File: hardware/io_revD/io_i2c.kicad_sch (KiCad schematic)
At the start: 50 parts, among them J1 Target Interface, 2716 Pinout, J2 Jumper Block, J3 Jumper Block, J4 Target Interface, 2716 Pinout, Q1 2N7000, U1 2716, U2 74HCT74, U3 74HCT125, U4 74HCT138, U6 MCP23018-E_SP, U7 74HCT138

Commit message: fixed pullup
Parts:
- removed R?: 1k, Resistor_THT:R_Axial_DIN0207_L6.3mm_D2.5mm_P2.54mm_Vertical, symbol Device:R
- added R?: 1k, Resistor_THT:R_Axial_DIN0207_L6.3mm_D2.5mm_P2.54mm_Vertical, symbol Device:R
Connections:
- net +5V: now also R?.1
- net at D1.2 (A), D2.2 (A), D3.2 (A)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: now also R?.2
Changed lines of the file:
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@@
   (junction (at 180.975 215.9) (diameter 0) (color 0 0 0 0)
   )
+  (junction (at 151.13 139.065) (diameter 0) (color 0 0 0 0)
+  )
   (junction (at 212.09 133.985) (diameter 0) (color 0 0 0 0)
   )
@@
   )
   (junction (at 185.42 80.645) (diameter 0) (color 0 0 0 0)
-  )
-  (junction (at 134.62 163.83) (diameter 0) (color 0 0 0 0)
   )
   (junction (at 212.09 159.385) (diameter 0) (color 0 0 0 0)
@@
     (stroke (width 0) (type default) (color 0 0 0 0))
   )
-  (wire (pts (xy 130.81 163.83) (xy 134.62 163.83))
-    (stroke (width 0) (type default) (color 0 0 0 0))
-  )
   (wire (pts (xy 246.38 32.385) (xy 246.38 33.655))
     (stroke (width 0) (type default) (color 0 0 0 0))
@@
     (stroke (width 0) (type default) (color 0 0 0 0))
   )
-  (wire (pts (xy 134.62 163.83) (xy 138.43 163.83))
+  (wire (pts (xy 130.81 163.83) (xy 138.43 163.83))
     (stroke (width 0) (type default) (color 0 0 0 0))
   )
@@
     (pin "1")
   )
-  (symbol (lib_id "power:+5V") (at 134.62 156.21 0) (unit 1)
-    (in_bom yes) (on_board yes)
-    (property "Reference" "#PWR?" (id 0) (at 134.62 160.02 0)
-      (effects (font (size 1.27 1.27)) hide)
-    )
-    (property "Value" "+5V" (id 1) (at 135.001 151.8158 0))
-    (property "Footprint" "" (id 2) (at 134.62 156.21 0)
-      (effects (font (size 1.27 1.27)) hide)
-    )
-    (property "Datasheet" "" (id 3) (at 134.62 156.21 0)
-      (effects (font (size 1.27 1.27)) hide)
-    )
-    (pin "1")
-  )
   (symbol (lib_id "74xx:74LS125") (at 43.815 76.2 0) (unit 2)
     (in_bom yes) (on_board yes)
@@
     )
     (pin "1")
+  )
+  (symbol (lib_id "Device:R") (at 151.13 135.255 0) (unit 1)
+    (in_bom yes) (on_board yes)
+    (property "Reference" "R?" (id 0) (at 147.32 133.985 0)
+      (effects (font (size 1.27 1.27)) (justify left))
+    )
+    (property "Value" "1k" (id 1) (at 147.32 136.525 0)
+      (effects (font (size 1.27 1.27)) (justify left))
+    )
+    (property "Footprint" "Resistor_THT:R_Axial_DIN0207_L6.3mm_D2.5mm_P2.54mm_Vertical" (id 2) (at 149.352 135.255 90)
+      (effects (font (size 1.27 1.27)) hide)
+    )
+    (property "Datasheet" "~" (id 3) (at 151.13 135.255 0)
+      (effects (font (size 1.27 1.27)) hide)
+    )
+    (pin "1")
+    (pin "2")
   )
   (symbol (lib_id "Diode:1N4148") (at 172.085 226.06 0) (unit 1)
@@
     (pin "1")
   )
-  (symbol (lib_id "Device:R") (at 134.62 160.02 0) (unit 1)
-    (in_bom yes) (on_board yes)
-    (property "Reference" "R?" (id 0) (at 130.81 158.75 0)
-      (effects (font (size 1.27 1.27)) (justify left))
-    )
-    (property "Value" "1k" (id 1) (at 130.81 161.29 0)
-      (effects (font (size 1.27 1.27)) (justify left))
-    )
-    (property "Footprint" "Resistor_THT:R_Axial_DIN0207_L6.3mm_D2.5mm_P2.54mm_Vertical" (id 2) (at 132.842 160.02 90)
-      (effects (font (size 1.27 1.27)) hide)
-    )
-    (property "Datasheet" "~" (id 3) (at 134.62 160.02 0)
-      (effects (font (size 1.27 1.27)) hide)
-    )
-    (pin "1")
-    (pin "2")
-  )
   (symbol (lib_id "Device:R") (at 232.41 91.44 0) (unit 1)
     (in_bom yes) (on_board yes)
@@
     )
     (property "Datasheet" "" (id 3) (at 102.87 61.595 0)
+      (effects (font (size 1.27 1.27)) hide)
+    )
+    (pin "1")
+  )
+  (symbol (lib_id "power:+5V") (at 151.13 131.445 0) (unit 1)
+    (in_bom yes) (on_board yes)
+    (property "Reference" "#PWR?" (id 0) (at 151.13 135.255 0)
+      (effects (font (size 1.27 1.27)) hide)
+    )
+    (property "Value" "+5V" (id 1) (at 151.511 127.0508 0))
+    (property "Footprint" "" (id 2) (at 151.13 131.445 0)
+      (effects (font (size 1.27 1.27)) hide)
+    )
+    (property "Datasheet" "" (id 3) (at 151.13 131.445 0)
       (effects (font (size 1.27 1.27)) hide)
     )
@@
       (reference "#PWR?") (unit 1) (value "GND") (footprint "")
     )
-    (path "/1f6a280c-02f7-41a2-af9f-44fb04f0a9b2"
-      (reference "#PWR?") (unit 1) (value "+5V") (footprint "")
-    )
     (path "/43879ac7-f230-4696-95ed-6babb22f0407"
       (reference "#PWR?") (unit 1) (value "+5V") (footprint "")
@@
       (reference "#PWR?") (unit 1) (value "+5V") (footprint "")
     )
+    (path "/8a404b86-d3e1-4be0-a8ba-be524434abfb"
+      (reference "#PWR?") (unit 1) (value "+5V") (footprint "")
+    )
     (path "/9147cd62-9ca6-4c6a-bf66-316c793b7506"
       (reference "#PWR?") (unit 1) (value "+5VD") (footprint "")
@@
       (reference "R5") (unit 1) (value "10k") (footprint "Resistor_THT:R_Axial_DIN0207_L6.3mm_D2.5mm_P2.54mm_Vertical")
     )
+    (path "/5191daa9-7512-4ab7-ba71-5f4cad956e0f"
+      (reference "R?") (unit 1) (value "1k") (footprint "Resistor_THT:R_Axial_DIN0207_L6.3mm_D2.5mm_P2.54mm_Vertical")
+    )
     (path "/59d70ba8-8901-43d7-9e71-45fc4d05f5dd"
       (reference "R?") (unit 1) (value "10k") (footprint "Resistor_THT:R_Axial_DIN0207_L6.3mm_D2.5mm_P2.54mm_Vertical")
@@
       (reference "R?") (unit 1) (value "4.7k") (footprint "Resistor_THT:R_Axial_DIN0207_L6.3mm_D2.5mm_P2.54mm_Vertical")
     )
-    (path "/857b2b5c-6887-40fa-8781-7287c485d91d"
-      (reference "R?") (unit 1) (value "1k") (footprint "Resistor_THT:R_Axial_DIN0207_L6.3mm_D2.5mm_P2.54mm_Vertical")
-    )
     (path "/00000000-0000-0000-0000-0000607df9f3"

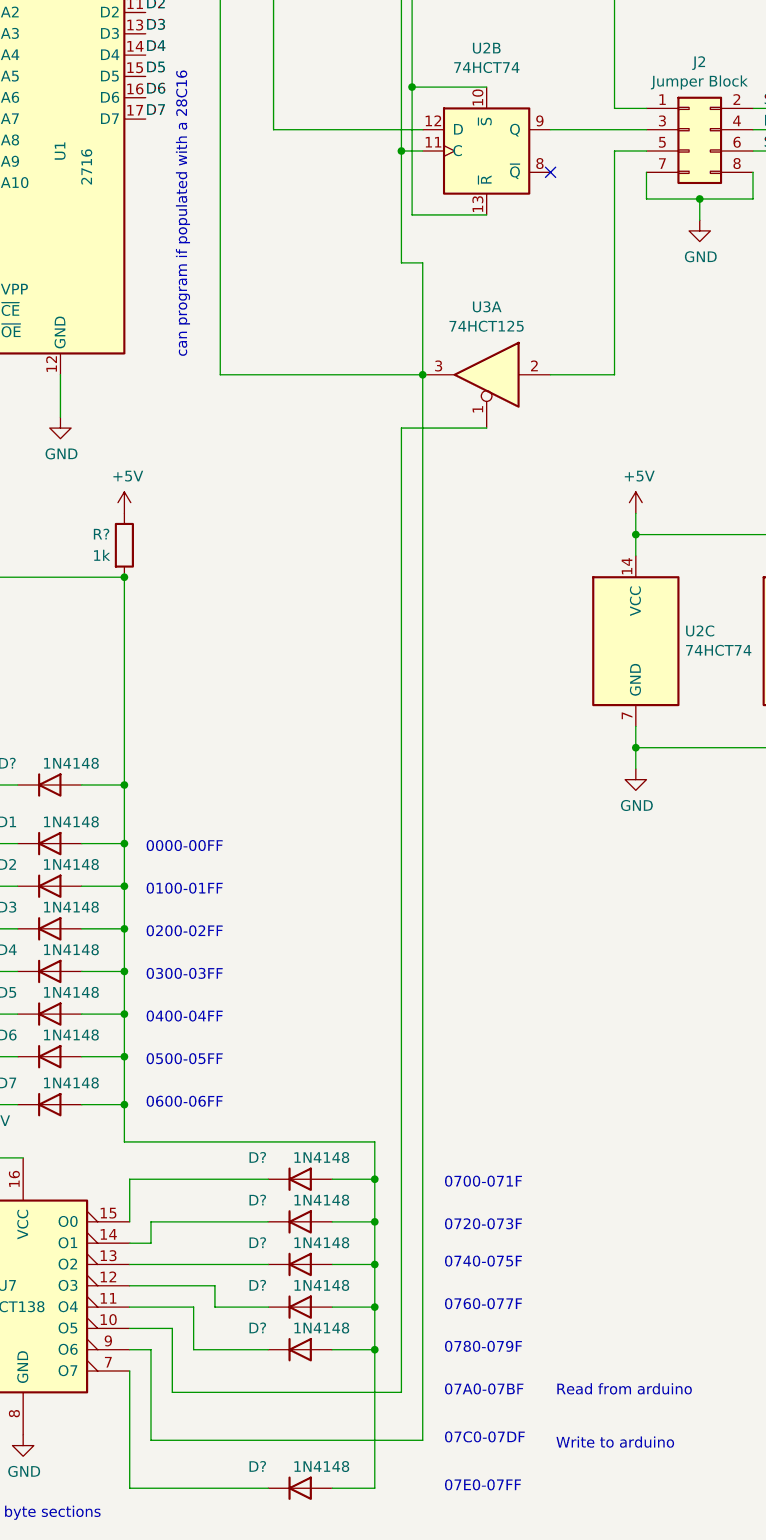
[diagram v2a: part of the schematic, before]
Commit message: fix crossed wires
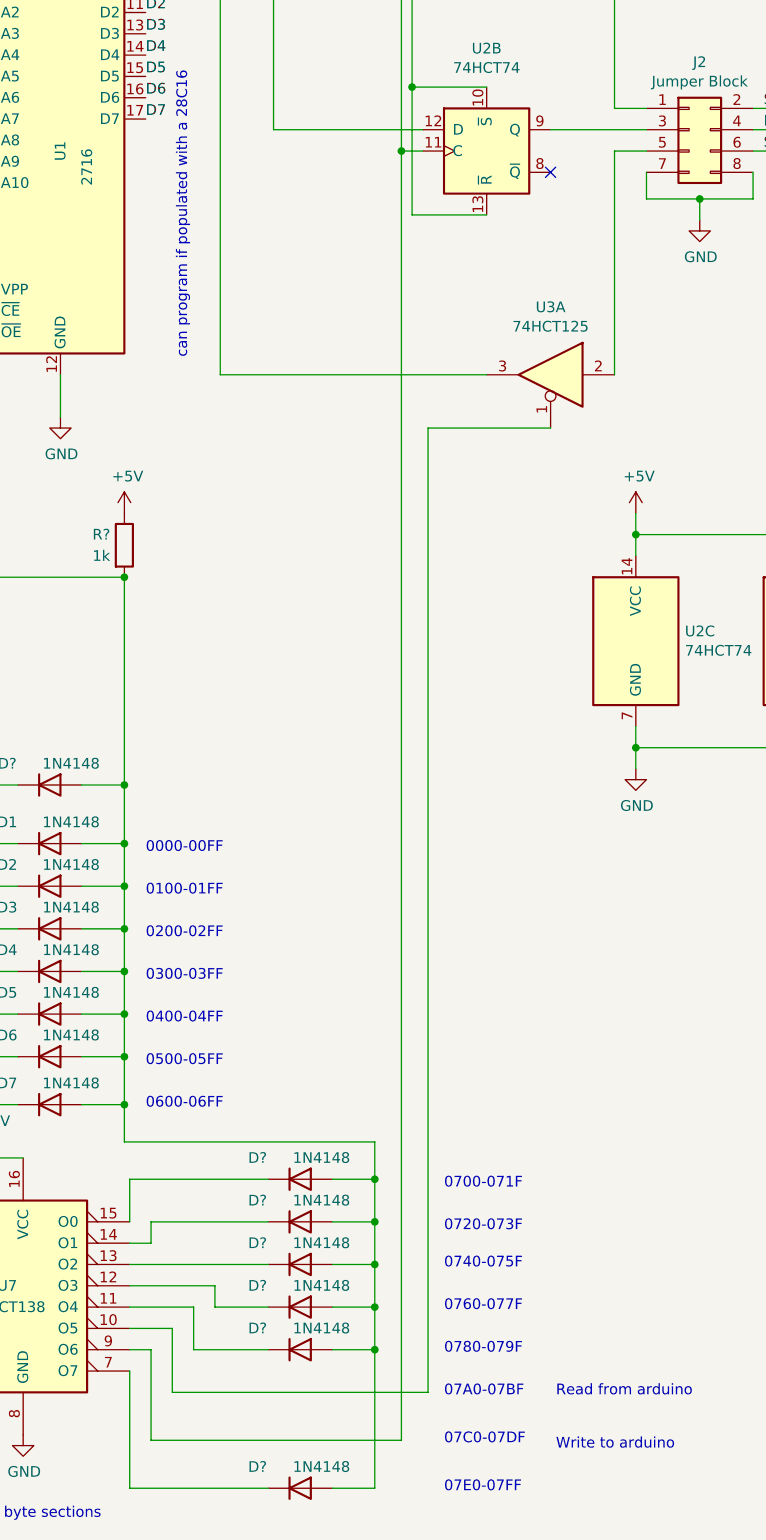
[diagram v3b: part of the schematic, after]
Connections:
- net D0: no longer U2.11 (C), U2.3 (C), U7.9 (O6)
- new net: U2.11 (C), U2.3 (C), U7.9 (O6)
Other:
- moved on the sheet: U3A
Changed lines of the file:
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@@
   (junction (at 252.73 93.345) (diameter 0) (color 0 0 0 0)
-  )
-  (junction (at 186.69 114.935) (diameter 0) (color 0 0 0 0)
   )
   (junction (at 180.975 215.9) (diameter 0) (color 0 0 0 0)
@@
     (stroke (width 0) (type default) (color 0 0 0 0))
   )
-  (wire (pts (xy 186.69 114.935) (xy 186.69 241.935))
-    (stroke (width 0) (type default) (color 0 0 0 0))
-  )
   (wire (pts (xy 256.54 156.21) (xy 262.89 156.21))
     (stroke (width 0) (type default) (color 0 0 0 0))
@@
     (stroke (width 0) (type default) (color 0 0 0 0))
   )
-  (wire (pts (xy 184.15 121.285) (xy 194.31 121.285))
-    (stroke (width 0) (type default) (color 0 0 0 0))
-  )
   (wire (pts (xy 154.305 218.44) (xy 154.305 215.9))
     (stroke (width 0) (type default) (color 0 0 0 0))
@@
     (stroke (width 0) (type default) (color 0 0 0 0))
   )
-  (wire (pts (xy 186.69 101.6) (xy 186.69 114.935))
-    (stroke (width 0) (type default) (color 0 0 0 0))
-  )
   (wire (pts (xy 92.71 109.855) (xy 90.17 109.855))
     (stroke (width 0) (type default) (color 0 0 0 0))
@@
     (stroke (width 0) (type default) (color 0 0 0 0))
   )
-  (wire (pts (xy 201.93 114.935) (xy 209.55 114.935))
-    (stroke (width 0) (type default) (color 0 0 0 0))
-  )
   (wire (pts (xy 212.09 156.845) (xy 212.09 159.385))
     (stroke (width 0) (type default) (color 0 0 0 0))
@@
     (stroke (width 0) (type default) (color 0 0 0 0))
   )
-  (wire (pts (xy 162.56 114.935) (xy 186.69 114.935))
+  (wire (pts (xy 162.56 114.935) (xy 194.31 114.935))
     (stroke (width 0) (type default) (color 0 0 0 0))
   )
@@
     (stroke (width 0) (type default) (color 0 0 0 0))
   )
-  (wire (pts (xy 184.15 236.22) (xy 184.15 121.285))
-    (stroke (width 0) (type default) (color 0 0 0 0))
-  )
   (wire (pts (xy 71.755 139.065) (xy 81.915 139.065))
     (stroke (width 0) (type default) (color 0 0 0 0))
@@
     (stroke (width 0) (type default) (color 0 0 0 0))
   )
-  (wire (pts (xy 184.15 101.6) (xy 186.69 101.6))
+  (wire (pts (xy 201.93 121.285) (xy 187.325 121.285))
     (stroke (width 0) (type default) (color 0 0 0 0))
   )
@@
     (stroke (width 0) (type default) (color 0 0 0 0))
   )
+  (wire (pts (xy 184.15 88.265) (xy 184.15 241.935))
+    (stroke (width 0) (type default) (color 0 0 0 0))
+  )
   (wire (pts (xy 151.13 201.93) (xy 151.13 196.215))
     (stroke (width 0) (type default) (color 0 0 0 0))
   )
+  (wire (pts (xy 187.325 121.285) (xy 187.325 236.22))
+    (stroke (width 0) (type default) (color 0 0 0 0))
+  )
   (wire (pts (xy 57.785 131.445) (xy 64.135 131.445))
     (stroke (width 0) (type default) (color 0 0 0 0))
@@
     (stroke (width 0) (type default) (color 0 0 0 0))
   )
-  (wire (pts (xy 184.15 88.265) (xy 184.15 101.6))
-    (stroke (width 0) (type default) (color 0 0 0 0))
-  )
   (wire (pts (xy 120.015 131.445) (xy 120.015 144.145))
     (stroke (width 0) (type default) (color 0 0 0 0))
@@
     (stroke (width 0) (type default) (color 0 0 0 0))
   )
-  (wire (pts (xy 156.845 236.22) (xy 184.15 236.22))
+  (wire (pts (xy 156.845 236.22) (xy 187.325 236.22))
     (stroke (width 0) (type default) (color 0 0 0 0))
   )
@@
     (stroke (width 0) (type default) (color 0 0 0 0))
   )
-  (wire (pts (xy 154.305 241.935) (xy 186.69 241.935))
+  (wire (pts (xy 154.305 241.935) (xy 184.15 241.935))
     (stroke (width 0) (type default) (color 0 0 0 0))
   )
@@
     (pin "9")
   )
-  (symbol (lib_id "74xx:74LS125") (at 194.31 114.935 0) (mirror y) (unit 1)
+  (symbol (lib_id "74xx:74LS125") (at 201.93 114.935 0) (mirror y) (unit 1)
     (in_bom yes) (on_board yes)
-    (property "Reference" "U3" (id 0) (at 194.31 106.8832 0))
-    (property "Value" "74HCT125" (id 1) (at 194.31 109.1946 0))
-    (property "Footprint" "Package_DIP:DIP-14_W7.62mm" (id 2) (at 194.31 114.935 0)
-      (effects (font (size 1.27 1.27)) hide)
-    )
-    (property "Datasheet" "http://www.ti.com/lit/gpn/sn74LS125" (id 3) (at 194.31 114.935 0)
-      (effects (font (size 1.27 1.27)) hide)
-    )
+    (property "Reference" "U3" (id 0) (at 201.93 106.8832 0))
+    (property "Value" "74HCT125" (id 1) (at 201.93 109.1946 0))
+    (property "Footprint" "Package_DIP:DIP-14_W7.62mm" (id 2) (at 201.93 114.935 0)
+      (effects (font (size 1.27 1.27)) hide)
+    )
+    (property "Datasheet" "http://www.ti.com/lit/gpn/sn74LS125" (id 3) (at 201.93 114.935 0)
+      (effects (font (size 1.27 1.27)) hide)
+    )

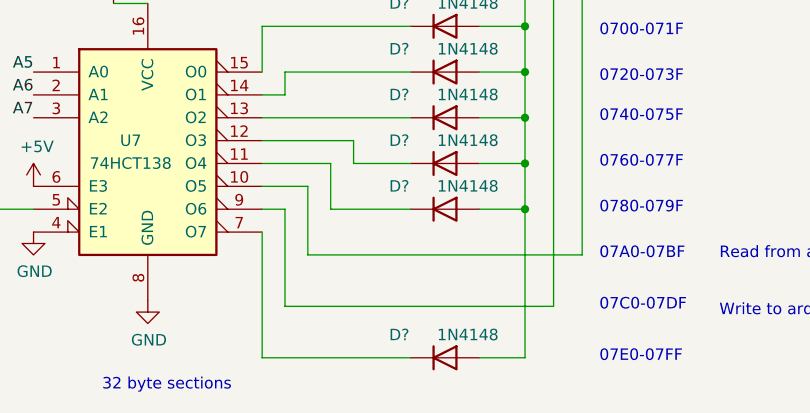
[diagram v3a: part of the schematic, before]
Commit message: diode fix for decoding writes
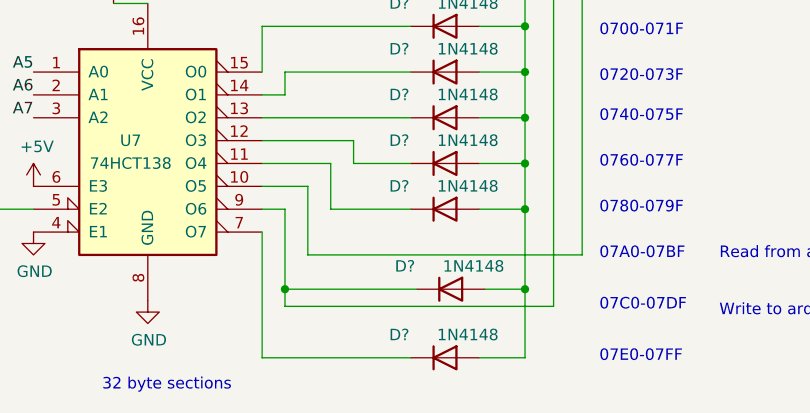
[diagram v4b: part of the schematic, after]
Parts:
- added D?: 1N4148, Diode_THT:D_DO-35_SOD27_P2.54mm_Vertical_AnodeUp, symbol Diode:1N4148
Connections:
- net at D1.2 (A), D2.2 (A), D3.2 (A)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: now also D?.2 (A)
- net at U2.11 (C), U2.3 (C), U7.9 (O6): now also D?.1 (K)
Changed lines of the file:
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@@
   (junction (at 212.09 133.985) (diameter 0) (color 0 0 0 0)
   )
+  (junction (at 154.305 240.03) (diameter 0) (color 0 0 0 0)
+  )
   (junction (at 125.73 104.775) (diameter 0) (color 0 0 0 0)
   )
@@
   )
   (junction (at 151.13 196.215) (diameter 0) (color 0 0 0 0)
+  )
+  (junction (at 180.975 240.03) (diameter 0) (color 0 0 0 0)
   )
   (junction (at 151.13 191.135) (diameter 0) (color 0 0 0 0)
@@
     (stroke (width 0) (type default) (color 0 0 0 0))
   )
+  (wire (pts (xy 154.305 240.03) (xy 154.305 231.14))
+    (stroke (width 0) (type default) (color 0 0 0 0))
+  )
   (wire (pts (xy 175.895 231.14) (xy 180.975 231.14))
     (stroke (width 0) (type default) (color 0 0 0 0))
@@
     (stroke (width 0) (type default) (color 0 0 0 0))
   )
+  (wire (pts (xy 154.305 240.03) (xy 168.91 240.03))
+    (stroke (width 0) (type default) (color 0 0 0 0))
+  )
   (wire (pts (xy 292.1 42.545) (xy 292.1 43.815))
     (stroke (width 0) (type default) (color 0 0 0 0))
@@
     (stroke (width 0) (type default) (color 0 0 0 0))
   )
-  (wire (pts (xy 154.305 241.935) (xy 154.305 231.14))
+  (wire (pts (xy 154.305 241.935) (xy 154.305 240.03))
     (stroke (width 0) (type default) (color 0 0 0 0))
   )
@@
     (stroke (width 0) (type default) (color 0 0 0 0))
   )
+  (wire (pts (xy 176.53 240.03) (xy 180.975 240.03))
+    (stroke (width 0) (type default) (color 0 0 0 0))
+  )
   (wire (pts (xy 175.895 215.9) (xy 180.975 215.9))
     (stroke (width 0) (type default) (color 0 0 0 0))
@@
     (stroke (width 0) (type default) (color 0 0 0 0))
   )
-  (wire (pts (xy 180.975 231.14) (xy 180.975 247.65))
+  (wire (pts (xy 180.975 240.03) (xy 180.975 247.65))
+    (stroke (width 0) (type default) (color 0 0 0 0))
+  )
+  (wire (pts (xy 180.975 231.14) (xy 180.975 240.03))
     (stroke (width 0) (type default) (color 0 0 0 0))
   )
@@
     (pin "2")
   )
+  (symbol (lib_id "Diode:1N4148") (at 172.72 240.03 0) (unit 1)
+    (in_bom yes) (on_board yes)
+    (property "Reference" "D?" (id 0) (at 167.64 237.49 0))
+    (property "Value" "1N4148" (id 1) (at 175.26 237.49 0))
+    (property "Footprint" "Diode_THT:D_DO-35_SOD27_P2.54mm_Vertical_AnodeUp" (id 2) (at 172.72 244.475 0)
+      (effects (font (size 1.27 1.27)) hide)
+    )
+    (property "Datasheet" "https://assets.nexperia.com/documents/data-sheet/1N4148_1N4448.pdf" (id 3) (at 172.72 240.03 0)
+      (effects (font (size 1.27 1.27)) hide)
+    )
+    (pin "1")
+    (pin "2")
+  )
   (symbol (lib_id "Device:C") (at 292.1 38.735 0) (unit 1)
     (in_bom yes) (on_board yes)
@@
       (reference "D?") (unit 1) (value "1N4148") (footprint "Diode_THT:D_DO-35_SOD27_P2.54mm_Vertical_AnodeUp")
     )
+    (path "/edb35209-55c3-49a8-9aaf-369715e21308"
+      (reference "D?") (unit 1) (value "1N4148") (footprint "Diode_THT:D_DO-35_SOD27_P2.54mm_Vertical_AnodeUp")
+    )
